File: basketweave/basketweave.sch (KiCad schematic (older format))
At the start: 175 parts, among them J1 AVR-ISP-6, SW1 SW_Push, SW2 SW_Push, SW3 Rotary_Encoder_Switch, U1 ATmega32A-PU, U2 GCT-USB-4085-GF-A, Y1 16Mhz

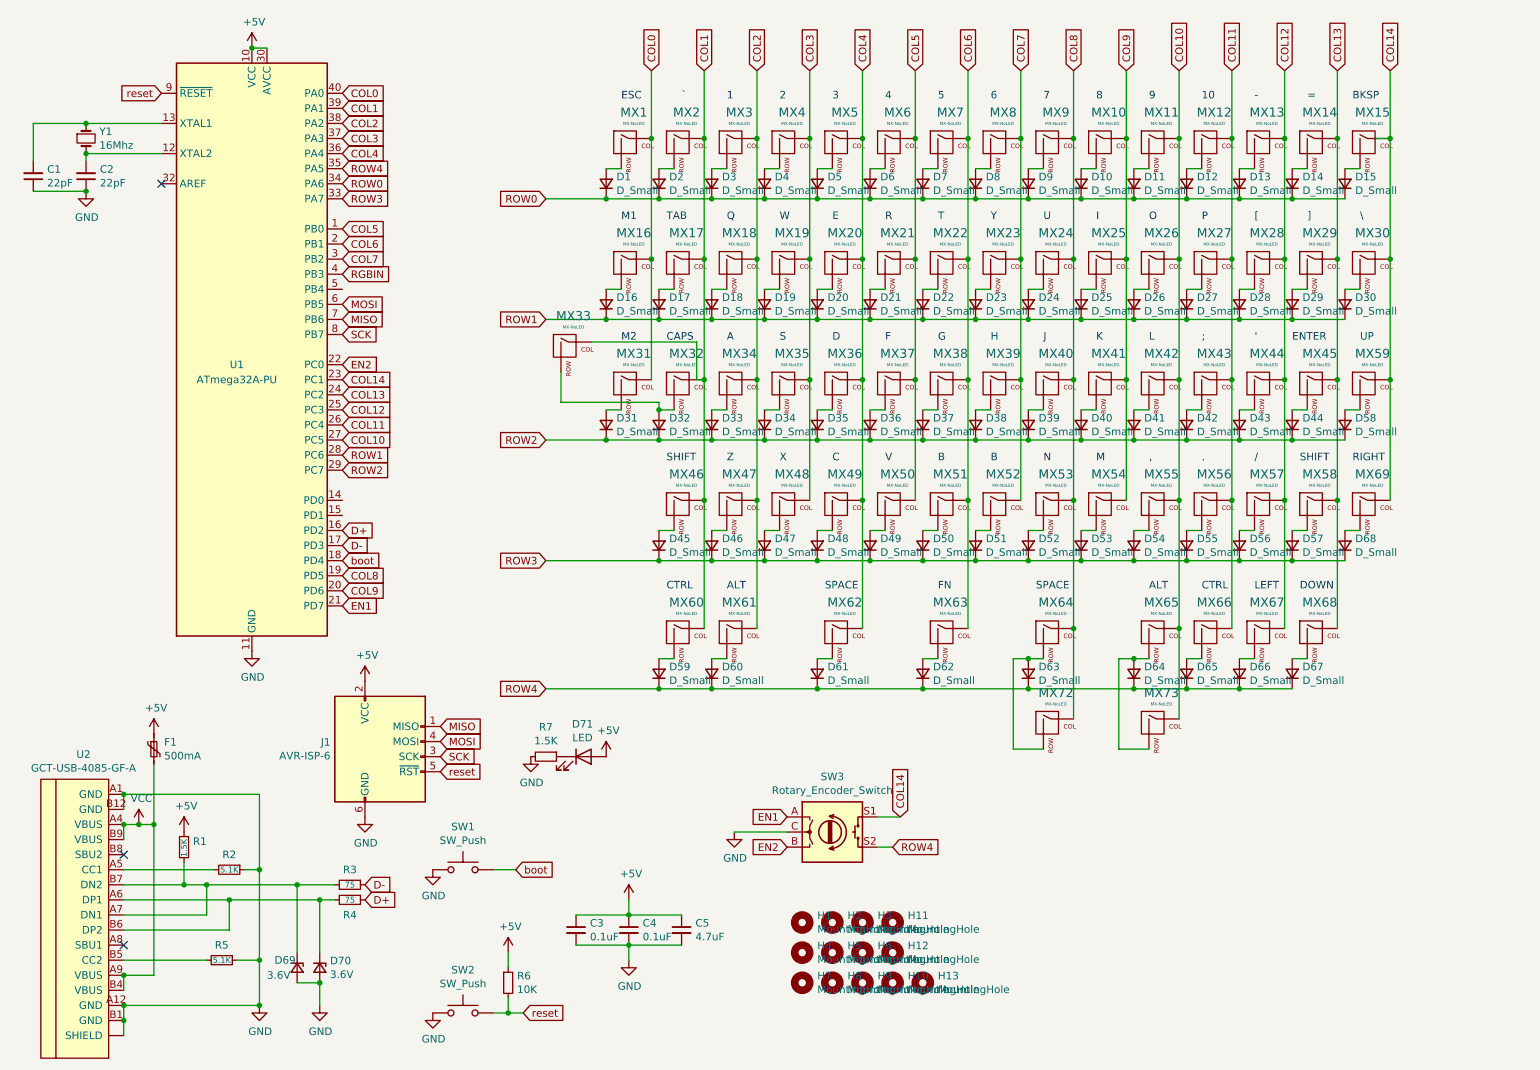
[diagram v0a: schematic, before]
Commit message: changed logo, name, and pattern design
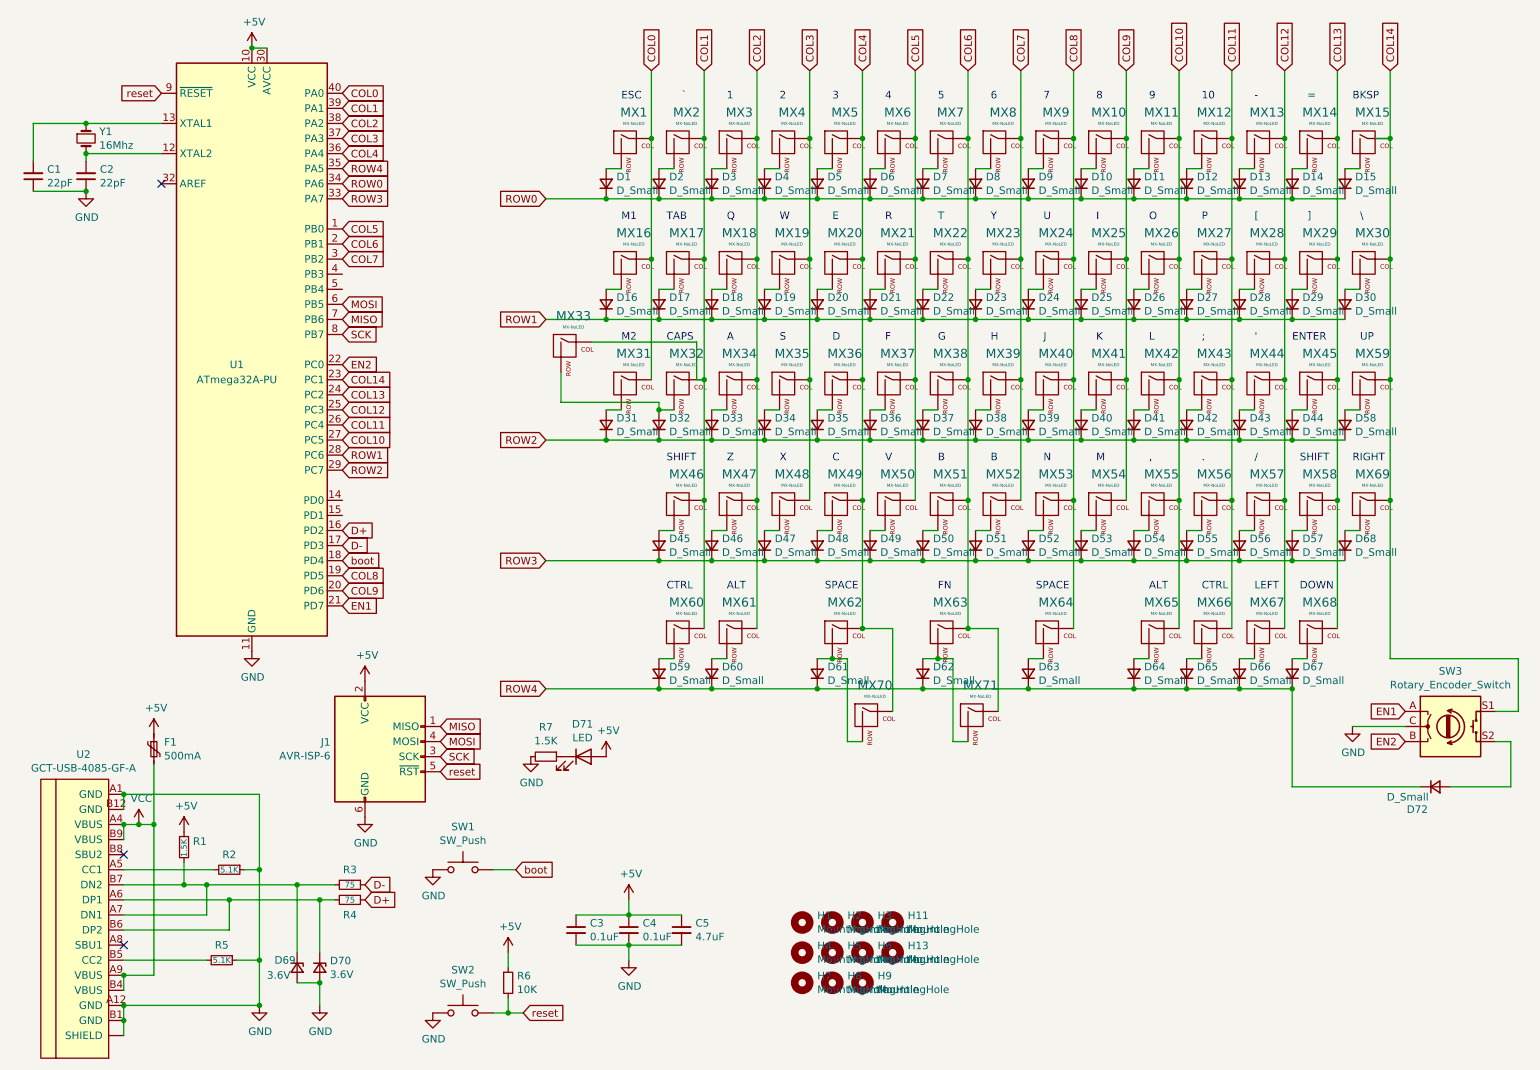
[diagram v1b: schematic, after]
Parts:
- removed H10, H12: MountingHole, MountingHole:MountingHole_2.2mm_M2_Pad, symbol Mechanical:MountingHole
- removed MX72: MX-NoLED, MX_Only:MXOnly-3U-ReversedStabilizers-NoLED, symbol keyboard-rescue:MX-NoLED-MX_Alps_Hybrid
- removed MX73: MX-NoLED, MX_Only:MXOnly-1.25U-NoLED, symbol keyboard-rescue:MX-NoLED-MX_Alps_Hybrid
- added D72: D_Small, Diode_THT:D_DO-35_SOD27_P7.62mm_Horizontal, symbol Device:D_Small
- added MX70: MX-NoLED, MX_Only:MXOnly-2.25U-ReversedStabilizers-NoLED, symbol keyboard-rescue:MX-NoLED-MX_Alps_Hybrid
- added MX71: MX-NoLED, MX_Only:MXOnly-1U-NoLED, symbol keyboard-rescue:MX-NoLED-MX_Alps_Hybrid
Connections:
- net COL4: now also MX70.1 (COL)
- net COL6: now also MX71.1 (COL)
- net ROW4: now also D72.1 (K); no longer SW3.S2
- net at D61.2 (A), MX62.2 (ROW): now also MX70.2 (ROW)
- net at D62.2 (A), MX63.2 (ROW): now also MX71.2 (ROW)
- net RGBIN: no longer names the net of U1.4 (PB3)
- new net: D72.2 (A), SW3.S2
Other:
- moved on the sheet: H13, SW3
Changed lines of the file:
@@
 	8750 4850 8650 4850
-$Comp
-L keyboard-rescue:MX-NoLED-MX_Alps_Hybrid MX68
-U 1 1 5F0877E7
-P 9150 4700
-F 0 "MX68" H 9183 4923 60  0000 C CNN
-F 1 "MX-NoLED" H 9183 4849 20  0000 C CNN
-F 2 "MX_Only:MXOnly-1U-NoLED" H 8525 4675 60  0001 C CNN
-F 3 "" H 8525 4675 60  0001 C CNN
-	1    9150 4700
-	1    0    0    -1
-$EndComp
 $Comp
 L Device:D_Small D67
@@
 Wire Wire Line
 	9100 4850 9000 4850
-$Comp
-L keyboard-rescue:MX-NoLED-MX_Alps_Hybrid MX69
-U 1 1 5F0877F4
-P 9500 3850
-F 0 "MX69" H 9533 4073 60  0000 C CNN
-F 1 "MX-NoLED" H 9533 3999 20  0000 C CNN
-F 2 "MX_Only:MXOnly-1U-NoLED" H 8875 3825 60  0001 C CNN
-F 3 "" H 8875 3825 60  0001 C CNN
-	1    9500 3850
-	1    0    0    -1
-$EndComp
 $Comp
 L Device:D_Small D68
@@
 	5150 3400 5500 3400
 Wire Wire Line
-	9300 3800 9300 3000
-Wire Wire Line
 	8650 3400 9000 3400
 Connection ~ 9000 4200
@@
 Wire Wire Line
 	7250 5050 7950 5050
-Connection ~ 9300 3800
-$Comp
-L keyboard-rescue:MX-NoLED-MX_Alps_Hybrid MX72
-U 1 1 5F0EB889
-P 7400 5300
-F 0 "MX72" H 7433 5523 60  0000 C CNN
-F 1 "MX-NoLED" H 7433 5449 20  0000 C CNN
-F 2 "MX_Only:MXOnly-3U-ReversedStabilizers-NoLED" H 6775 5275 60  0001 C CNN
-F 3 "" H 6775 5275 60  0001 C CNN
-	1    7400 5300
-	1    0    0    -1
-$EndComp
-Wire Wire Line
-	7550 5250 7550 4650
-Connection ~ 7550 4650
-Wire Wire Line
-	7350 5450 7150 5450
-Wire Wire Line
-	7150 5450 7150 4850
-Wire Wire Line
-	7150 4850 7250 4850
-Connection ~ 7250 4850
-$Comp
-L keyboard-rescue:MX-NoLED-MX_Alps_Hybrid MX73
-U 1 1 5F129B15
-P 8100 5300
-F 0 "MX73" H 8133 5523 60  0000 C CNN
-F 1 "MX-NoLED" H 8133 5449 20  0000 C CNN
-F 2 "MX_Only:MXOnly-1.25U-NoLED" H 7475 5275 60  0001 C CNN
-F 3 "" H 7475 5275 60  0001 C CNN
-	1    8100 5300
-	1    0    0    -1
-$EndComp
-Wire Wire Line
-	8250 5250 8250 4650
-Connection ~ 8250 4650
-Wire Wire Line
-	8050 5450 7850 5450
-Wire Wire Line
-	7850 5450 7850 4850
-Wire Wire Line
-	7850 4850 7950 4850
-Connection ~ 7950 4850
 Text GLabel 2700 1700 2    50   Input ~ 0
 ROW0
@@
 	9650 3000 9650 3800
 Wire Wire Line
-	9300 3800 9300 4650
-Wire Wire Line
 	7950 5050 8300 5050
 Text GLabel 2700 3000 2    50   Input ~ 0
 COL14
-Text GLabel 2700 2300 2    50   Input ~ 0
-RGBIN
 Text GLabel 2700 3500 2    50   Input ~ 0
 ROW1
@@
 	8650 5050 9000 5050
 Connection ~ 8950 3800
-Text GLabel 5650 6100 0    50   Input ~ 0
+Text GLabel 9750 5400 0    50   Input ~ 0
 EN2
-Text GLabel 5650 5900 0    50   Input ~ 0
+Text GLabel 9750 5200 0    50   Input ~ 0
 EN1
 Wire Wire Line
-	5650 6000 5300 6000
+	9750 5300 9400 5300
 $Comp
 L power:GND #PWR0107
 U 1 1 5FF51463
-P 5300 6000
-F 0 "#PWR0107" H 5300 5750 50  0001 C CNN
-F 1 "GND" H 5305 5827 50  0000 C CNN
-F 2 "" H 5300 6000 50  0001 C CNN
-F 3 "" H 5300 6000 50  0001 C CNN
-	1    5300 6000
+P 9400 5300
+F 0 "#PWR0107" H 9400 5050 50  0001 C CNN
+F 1 "GND" H 9405 5127 50  0000 C CNN
+F 2 "" H 9400 5300 50  0001 C CNN
+F 3 "" H 9400 5300 50  0001 C CNN
+	1    9400 5300
 	1    0    0    -1
 $EndComp
@@
 L Device:Rotary_Encoder_Switch SW3
 U 1 1 5FEF8062
-P 5950 6000
-F 0 "SW3" H 5950 6367 50  0000 C CNN
-F 1 "Rotary_Encoder_Switch" H 5950 6276 50  0000 C CNN
-F 2 "Rotary_Encoder:RotaryEncoder_Alps_EC11E-Switch_Vertical_H20mm" H 5800 6160 50  0001 C CNN
-F 3 "~" H 5950 6260 50  0001 C CNN
-	1    5950 6000
-	1    0    0    -1
-$EndComp
-Text GLabel 6400 5900 1    50   Input ~ 0
-COL14
-Text GLabel 6350 6100 2    50   Input ~ 0
-ROW4
-Wire Wire Line
-	6250 5900 6400 5900
-Wire Wire Line
-	6250 6100 6350 6100
+P 10050 5300
+F 0 "SW3" H 10050 5667 50  0000 C CNN
+F 1 "Rotary_Encoder_Switch" H 10050 5576 50  0000 C CNN
+F 2 "Rotary_Encoder:RotaryEncoder_Alps_EC11E-Switch_Vertical_H20mm" H 9900 5460 50  0001 C CNN
+F 3 "~" H 10050 5560 50  0001 C CNN
+	1    10050 5300
+	1    0    0    -1
+$EndComp
+Wire Wire Line
+	10350 5200 10500 5200
+Wire Wire Line
+	10350 5400 10450 5400
 Text GLabel 2700 4500 2    50   Input ~ 0
 EN1
@@
 	1    0    0    -1
 $EndComp
-$Comp
-L Mechanical:MountingHole H10
-U 1 1 5F1FE900
-P 6350 7000
-F 0 "H10" H 6450 7046 50  0000 L CNN
-F 1 "MountingHole" H 6450 6955 50  0000 L CNN
-F 2 "MountingHole:MountingHole_2.2mm_M2_Pad" H 6350 7000 50  0001 C CNN
-F 3 "~" H 6350 7000 50  0001 C CNN
-	1    6350 7000
-	1    0    0    -1
-$EndComp
-$Comp
-L Mechanical:MountingHole H12
-U 1 1 5F2C5358
-P 6350 6800
-F 0 "H12" H 6450 6846 50  0000 L CNN
-F 1 "MountingHole" H 6450 6755 50  0000 L CNN
-F 2 "MountingHole:MountingHole_2.2mm_M2_Pad" H 6350 6800 50  0001 C CNN
-F 3 "~" H 6350 6800 50  0001 C CNN
-	1    6350 6800
-	1    0    0    -1
-$EndComp
 Wire Wire Line
 	9550 1400 9650 1400
@@
 $EndComp
 $Comp
+L Device:D_Small D72
+U 1 1 5F9801E6
+P 9950 5700
+F 0 "D72" H 9900 5550 50  0000 R CNN
+F 1 "D_Small" H 9905 5632 50  0000 R CNN
+F 2 "Diode_THT:D_DO-35_SOD27_P7.62mm_Horizontal" V 9950 5700 50  0001 C CNN
+F 3 "~" V 9950 5700 50  0001 C CNN
+	1    9950 5700
+	1    0    0    -1
+$EndComp
+Wire Wire Line
+	10050 5700 10450 5700
+Wire Wire Line
+	10450 5700 10450 5400
+Wire Wire Line
+	10500 5200 10500 4850
+Wire Wire Line
+	9850 5700 9000 5700
+Wire Wire Line
+	9000 5700 9000 5050
+Connection ~ 9000 5050
+$Comp
 L Mechanical:MountingHole H13
 U 1 1 5F56C269
-P 6550 7000
-F 0 "H13" H 6650 7046 50  0000 L CNN
-F 1 "MountingHole" H 6650 6955 50  0000 L CNN
-F 2 "MountingHole:MountingHole_2.2mm_M2_Pad" H 6550 7000 50  0001 C CNN
-F 3 "~" H 6550 7000 50  0001 C CNN
-	1    6550 7000
-	1    0    0    -1
-$EndComp
+P 6350 6800
+F 0 "H13" H 6450 6846 50  0000 L CNN
+F 1 "MountingHole" H 6450 6755 50  0000 L CNN
+F 2 "MountingHole:MountingHole_2.2mm_M2_Pad" H 6350 6800 50  0001 C CNN
+F 3 "~" H 6350 6800 50  0001 C CNN
+	1    6350 6800
+	1    0    0    -1
+$EndComp
+$Comp
+L keyboard-rescue:MX-NoLED-MX_Alps_Hybrid MX68
+U 1 1 5F0877E7
+P 9150 4700
+F 0 "MX68" H 9183 4923 60  0000 C CNN
+F 1 "MX-NoLED" H 9183 4849 20  0000 C CNN
+F 2 "MX_Only:MXOnly-1U-NoLED" H 8525 4675 60  0001 C CNN
+F 3 "" H 8525 4675 60  0001 C CNN
+	1    9150 4700
+	1    0    0    -1
+$EndComp
+$Comp
+L keyboard-rescue:MX-NoLED-MX_Alps_Hybrid MX69
+U 1 1 5F0877F4
+P 9500 3850
+F 0 "MX69" H 9533 4073 60  0000 C CNN
+F 1 "MX-NoLED" H 9533 3999 20  0000 C CNN
+F 2 "MX_Only:MXOnly-1U-NoLED" H 8875 3825 60  0001 C CNN
+F 3 "" H 8875 3825 60  0001 C CNN
+	1    9500 3850
+	1    0    0    -1
+$EndComp
+Wire Wire Line
+	9650 3800 9650 4850
+Wire Wire Line
+	9650 4850 10500 4850
+Connection ~ 9650 3800
+Wire Wire Line
+	9300 3000 9300 3800
+Connection ~ 9300 3800
+Wire Wire Line
+	9300 3800 9300 4650
+$Comp
+L keyboard-rescue:MX-NoLED-MX_Alps_Hybrid MX71
+U 1 1 5F95CADB
+P 6900 5250
+F 0 "MX71" H 6933 5473 60  0000 C CNN
+F 1 "MX-NoLED" H 6933 5399 20  0000 C CNN
+F 2 "MX_Only:MXOnly-1U-NoLED" H 6275 5225 60  0001 C CNN
+F 3 "" H 6275 5225 60  0001 C CNN
+	1    6900 5250
+	1    0    0    -1
+$EndComp
+Wire Wire Line
+	6650 4850 6750 4850
+Wire Wire Line
+	6750 4850 6750 5400
+Connection ~ 6650 4850
+Wire Wire Line
+	6750 5400 6850 5400
+Wire Wire Line
+	7050 5200 7050 4650
+Wire Wire Line
+	7050 4650 6850 4650
+Connection ~ 6850 4650
+$Comp
+L keyboard-rescue:MX-NoLED-MX_Alps_Hybrid MX70
+U 1 1 5F99CEF2
+P 6200 5250
+F 0 "MX70" H 6233 5473 60  0000 C CNN
+F 1 "MX-NoLED" H 6233 5399 20  0000 C CNN
+F 2 "MX_Only:MXOnly-2.25U-ReversedStabilizers-NoLED" H 5575 5225 60  0001 C CNN
+F 3 "" H 5575 5225 60  0001 C CNN
+	1    6200 5250
+	1    0    0    -1
+$EndComp
+Wire Wire Line
+	6150 4650 6350 4650
+Wire Wire Line
+	6350 4650 6350 5200
+Connection ~ 6150 4650
+Wire Wire Line
+	5950 4850 6050 4850
+Wire Wire Line
+	6050 4850 6050 5400
+Connection ~ 5950 4850
+Wire Wire Line
+	6050 5400 6150 5400
 $EndSCHEMATC

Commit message: fixed missing symbols
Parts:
- MX1, MX10, MX11, MX12, MX13, MX14, MX15, MX16, MX17, MX18, MX19, MX2, MX20, MX21, MX22, MX23, MX24, MX25, MX26, MX27, MX28, MX29, MX3, MX30, MX31, MX32, MX33, MX34, MX35, MX36, MX37, MX38, MX39, MX4, MX40, MX41, MX42, MX43, MX44, MX45, MX46, MX47, MX48, MX49, MX5, MX50, MX51, MX52, MX53, MX54, MX55, MX56, MX57, MX58, MX59, MX6, MX60, MX61, MX62, MX63, MX64, MX65, MX66, MX67, MX68, MX69, MX7, MX70, MX71, MX8, MX9: symbol keyboard-rescue:MX-NoLED-MX_Alps_Hybrid -> MX_Alps_Hybrid:MX-NoLED
- U2: symbol keyboard-rescue:GCT-USB-4085-GF-A-Type-C -> Type-C:GCT-USB-4085-GF-A
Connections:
- net COL0: no longer MX1.1 (COL), MX16.1 (COL)
- net COL1: no longer MX17.1 (COL), MX2.1 (COL), MX46.1 (COL)
- net COL10: no longer MX11.1 (COL), MX26.1 (COL), MX42.1 (COL), MX55.1 (COL)
- net COL11: no longer MX12.1 (COL), MX27.1 (COL), MX43.1 (COL), MX56.1 (COL)
- net COL12: no longer MX13.1 (COL), MX28.1 (COL), MX44.1 (COL), MX57.1 (COL)
- net COL13: no longer MX14.1 (COL), MX29.1 (COL), MX45.1 (COL), MX58.1 (COL)
- net COL14: no longer MX30.1 (COL), MX59.1 (COL), MX69.1 (COL)
- net COL2: no longer MX18.1 (COL), MX34.1 (COL), MX47.1 (COL)
- net COL3: no longer MX19.1 (COL), MX35.1 (COL), MX4.1 (COL)
- net COL4: no longer MX20.1 (COL), MX36.1 (COL), MX49.1 (COL), MX5.1 (COL)
- net COL5: no longer MX21.1 (COL), MX37.1 (COL), MX6.1 (COL)
- net COL6: no longer MX22.1 (COL), MX38.1 (COL), MX51.1 (COL), MX7.1 (COL)
- net COL7: no longer MX23.1 (COL), MX39.1 (COL), MX8.1 (COL)
- net COL8: no longer MX24.1 (COL), MX40.1 (COL), MX53.1 (COL), MX9.1 (COL)
- net COL9: no longer MX10.1 (COL), MX25.1 (COL), MX41.1 (COL)
- net GND: no longer U2.B1 (GND)
- net at D61.2 (A), MX70.2 (ROW): no longer MX62.2 (ROW)
- net at D62.2 (A), MX71.2 (ROW): no longer MX63.2 (ROW)
